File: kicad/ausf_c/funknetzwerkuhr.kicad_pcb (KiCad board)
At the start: 2 copper layers, 170.8 x 131.9 mm, 119 parts, among them J1 Jack-DC, J2 Conn_01x26_Male, J3 Conn_01x26_Female, J4 Conn_01x04_Male, Q1 IRF640, Q10 MMBTA42, Q11 MMBTA42, Q12 MMBTA42, Q13 MMBTA42, Q14 MMBTA42, Q15 MMBTA42, Q16 MMBTA42, Q17 MMBTA42, Q18 MMBTA42, Q19 MMBTA42, Q2 MMBTA42, Q20 MMBTA42, Q21 MMBTA42, Q22 MMBTA42, Q3 MMBTA92, Q4 MMBTA42, Q5 MMBTA92, Q6 MMBTA42, Q7 MMBTA92, Q8 MMBTA42, Q9 MMBTA92, T1 IN-12, T2 IN-12, T3 IN-12, T4 IN-12, U1 74HC595, U10 THERMAL_VIA, U11 THERMAL_VIA, U12 THERMAL_VIA, U13 THERMAL_VIA, U14 THERMAL_VIA, U15 THERMAL_VIA, U16 THERMAL_VIA, U2 74HC595, U3 74HC595, U4 max1771, U5 NCP1117-33G, U6 ESP-12E, U7 THERMAL_VIA, U8 THERMAL_VIA, U9 THERMAL_VIA

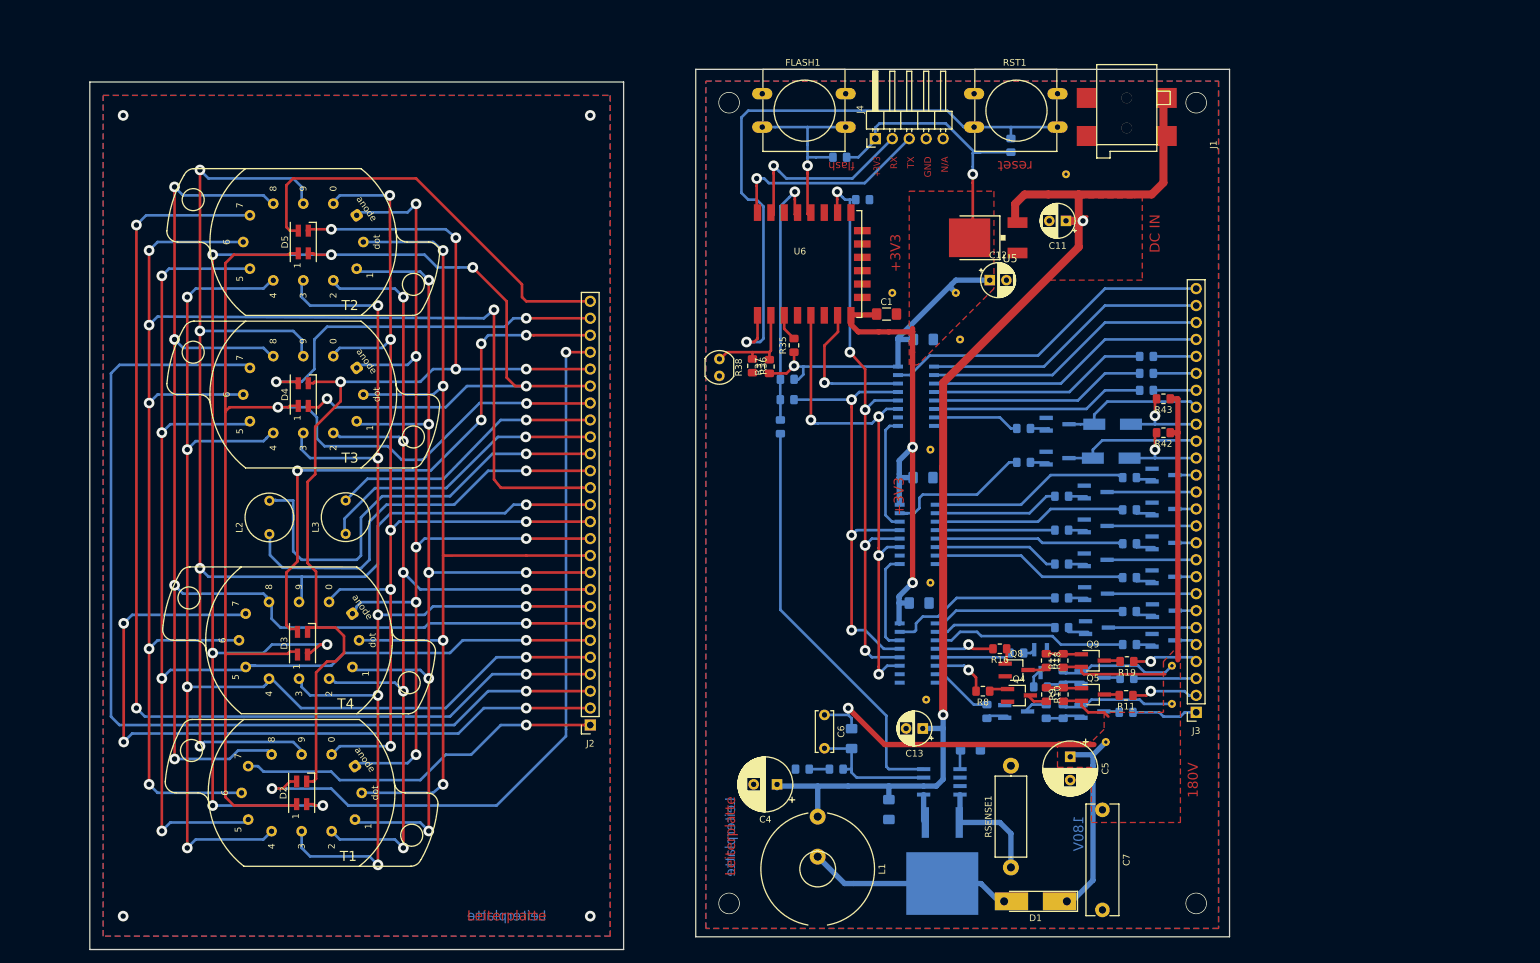
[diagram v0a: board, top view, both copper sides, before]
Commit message: PSU does not fit into the outline.
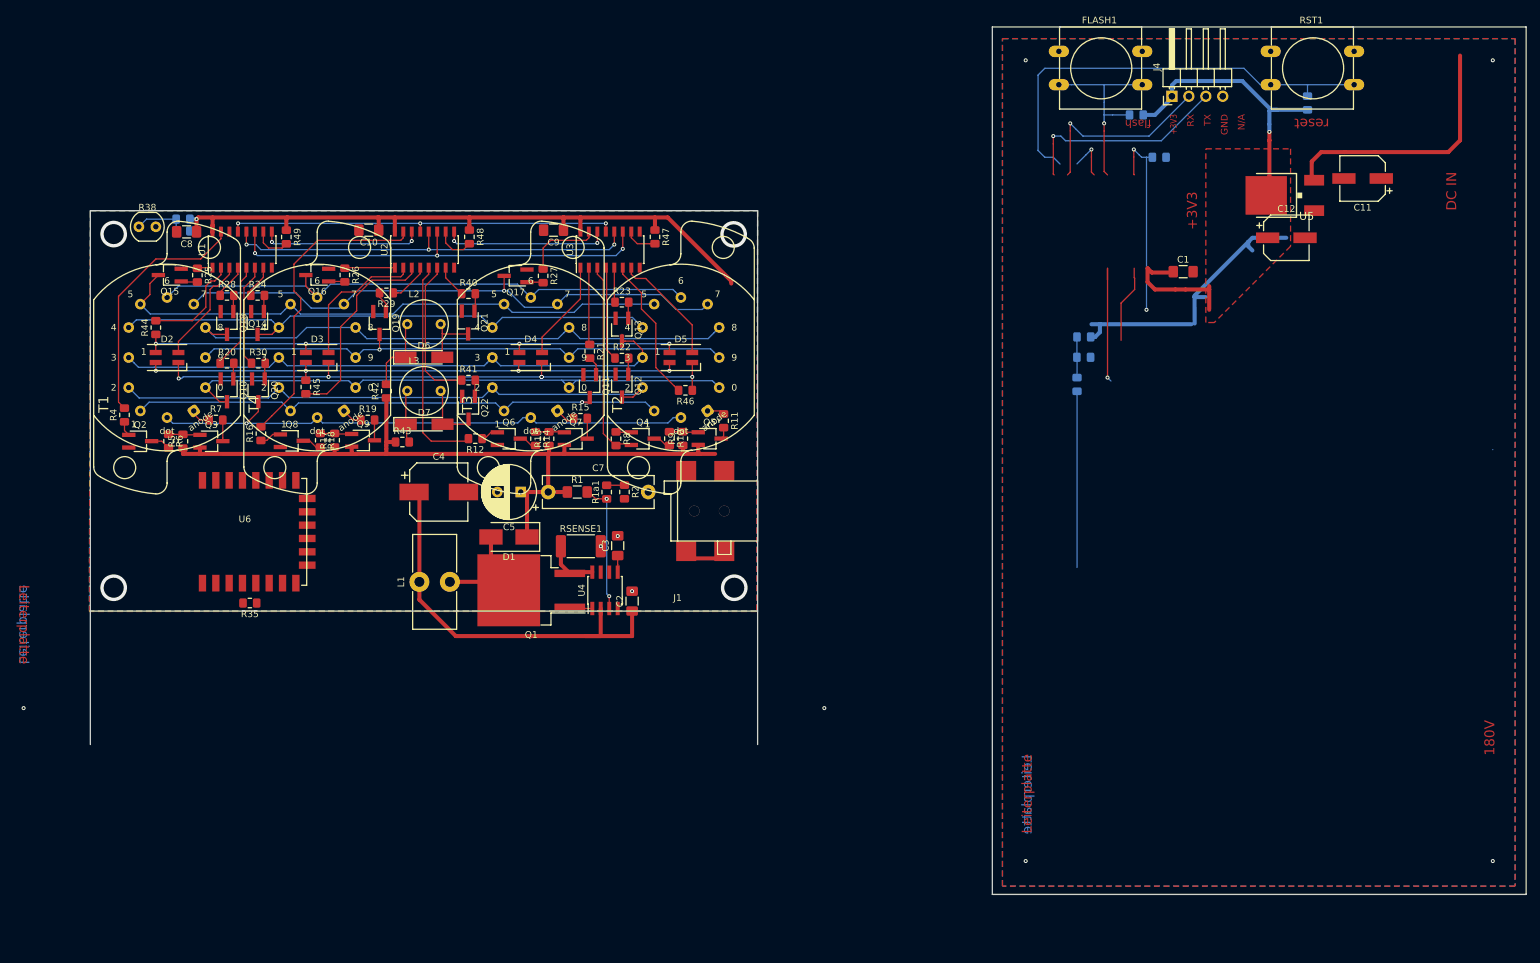
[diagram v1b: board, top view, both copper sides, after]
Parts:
- removed C13: 10uF,25V, Capacitor_THT:CP_Radial_D5.0mm_P2.50mm
- removed C6: 100p 1kV, Capacitor_THT:C_Disc_D6.0mm_W2.5mm_P5.00mm
- removed J2: Conn_01x26_Male, Connector_PinSocket_2.54mm:PinSocket_1x26_P2.54mm_Vertical
- removed J3: Conn_01x26_Female, Connector_PinSocket_2.54mm:PinSocket_1x26_P2.54mm_Vertical
- removed U10, U11, U12, U13, U14, U15, U16, U7, U8, U9: THERMAL_VIA, PartsStash_RW:Thermal_Via
- added R47: 10k, Resistor_SMD:R_0805_2012Metric_Pad1.15x1.40mm_HandSolder, F.Cu at (134.6, 58.9)
- added R48: 10k, Resistor_SMD:R_0805_2012Metric_Pad1.15x1.40mm_HandSolder, F.Cu at (106.8, 58.9)
- added R49: 10k, Resistor_SMD:R_0805_2012Metric_Pad1.15x1.40mm_HandSolder, F.Cu at (79.4, 58.9)
- C10, C2, C3, C8, C9, D6, D7, Q1, Q10, Q11, Q12, Q13, Q14, Q15, Q16, Q17, Q18, Q19, Q2, Q20, Q21, Q22, Q3, Q6, Q7, R1, R12, R13, R14, R15, R1a1, R2, R20, R21, R22, R23, R24, R25, R26, R27, R28, R29, R30, R4, R40, R41, R44, R45, R46, R5, R6, R7, U1, U2, U3, U4: moved to F.Cu
- C11, C12: footprint Capacitor_THT:CP_Radial_D5.0mm_P2.50mm -> Capacitor_SMD:CP_Elec_6.3x5.4
- C4: footprint Capacitor_THT:CP_Radial_D8.0mm_P3.50mm -> Capacitor_SMD:CP_Elec_8x10.5
- D1: footprint Parts:D_MELF-RM10_Universal_Handsoldering -> Diode_SMD:D_SMB_Handsoldering
- J4: footprint Connector_PinHeader_2.54mm:PinHeader_1x05_P2.54mm_Horizontal -> Connector_PinHeader_2.54mm:PinHeader_1x04_P2.54mm_Horizontal
- L1: footprint PartsStash_RW:L_Toroid_Horizontal_D16.8mm_P6mm_AliExpress -> Inductor_THT:L_Toroid_Vertical_L14.0mm_W6.3mm_P4.57mm_Pulse_A
- R36, R37: moved to B.Cu
- RSENSE1: footprint Resistor_THT:R_Axial_DIN0414_L11.9mm_D4.5mm_P15.24mm_Horizontal -> Resistor_SMD:R_2512_6332Metric_Pad1.52x3.35mm_HandSolder
- moved R44 148.8 mm to (59.8, 72.5), turned to 90 degrees
- moved Q15 148.7 mm to (61.9, 64.6), turned to 180 degrees
- moved Q18 146.9 mm to (70.5, 71.8), turned to 270 degrees
- moved Q14 143.9 mm to (75.1, 71.8), turned to 270 degrees
- moved R28 143.3 mm to (70.5, 67.7)
- moved R7 143.3 mm to (68.8, 86.4), turned to 0 degrees
- moved Q10 141.5 mm to (70.5, 81.9), turned to 270 degrees
- moved R24 140.8 mm to (75.1, 67.7)
- moved R25 139.9 mm to (66.0, 64.7), turned to 270 degrees
- moved Q3 138.1 mm to (68.1, 89.5)
- moved R5 138.0 mm to (63.9, 89.5), turned to 90 degrees
- moved R6 137.6 mm to (61.7, 89.5), turned to 270 degrees
- moved Q20 137.5 mm to (75.2, 81.9), turned to 270 degrees
- moved Q2 137.4 mm to (57.5, 89.5)
- moved R20 137.0 mm to (70.5, 77.9)
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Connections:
- net Net-(Q1-Pad3) renamed /hv_psu/SENSE
- net Net-(R33-Pad1) renamed /~OE
- net Net-(U1-Pad9) renamed /SERIAL_U2
- net Net-(U2-Pad9) renamed /SERIAL_U3
- D2 pad 1: Net-(D2-Pad1) -> /RED
- D2 pad 2: Net-(D2-Pad2) -> /DRIVE_LED_A1
- D2 pad 3: Net-(D2-Pad3) -> /GREEN
- D2 pad 4: Net-(D2-Pad4) -> /BLUE
- D3 pad 1: Net-(D2-Pad1) -> /RED
- D3 pad 2: Net-(D3-Pad2) -> /DRIVE_LED_A2
- D3 pad 3: Net-(D2-Pad3) -> /GREEN
- D3 pad 4: Net-(D2-Pad4) -> /BLUE
- D4 pad 1: Net-(D2-Pad1) -> /RED
- D4 pad 2: Net-(D4-Pad2) -> /DRIVE_LED_A3
- D4 pad 3: Net-(D2-Pad3) -> /GREEN
- D4 pad 4: Net-(D2-Pad4) -> /BLUE
- D5 pad 1: Net-(D2-Pad1) -> /RED
- D5 pad 2: Net-(D5-Pad2) -> /DRIVE_LED_A4
- D5 pad 3: Net-(D2-Pad3) -> /GREEN
- D5 pad 4: Net-(D2-Pad4) -> /BLUE
- L2 pad 1: Net-(J2-Pad16) -> /ANODE_N1
- L2 pad 2: Net-(J2-Pad17) -> /CATHODE_N1
- L3 pad 1: Net-(J2-Pad18) -> /ANODE_N2
- L3 pad 2: Net-(J2-Pad19) -> /CATHODE_N2
- R11 pad 1: /A2 -> /A4
- R16 pad 2: /DRIVE_A4 -> /DRIVE_A2
- R19 pad 1: /A4 -> /A2
- R8 pad 2: /DRIVE_A2 -> /DRIVE_A4
- T1 pad 1: /front_panel/A1 -> /A1
- T1 pad 10: /front_panel/D2 -> /D2
- T1 pad 11: /front_panel/D1 -> /D1
- T1 pad 12: /front_panel/DOT -> /DOT
- T1 pad 2: /front_panel/D0 -> /D0
- T1 pad 3: /front_panel/D9 -> /D9
- T1 pad 4: /front_panel/D8 -> /D8
- T1 pad 5: /front_panel/D7 -> /D7
- T1 pad 6: /front_panel/D6 -> /D6
- T1 pad 7: /front_panel/D5 -> /D5
- T1 pad 8: /front_panel/D4 -> /D4
- T1 pad 9: /front_panel/D3 -> /D3
- T2 pad 1: /front_panel/A2 -> /A4
- T2 pad 10: /front_panel/D2 -> /D2
- T2 pad 11: /front_panel/D1 -> /D1
- T2 pad 12: /front_panel/DOT -> /DOT
- T2 pad 2: /front_panel/D0 -> /D0
- T2 pad 3: /front_panel/D9 -> /D9
- T2 pad 4: /front_panel/D8 -> /D8
- T2 pad 5: /front_panel/D7 -> /D7
- T2 pad 6: /front_panel/D6 -> /D6
- T2 pad 7: /front_panel/D5 -> /D5
- T2 pad 8: /front_panel/D4 -> /D4
- T2 pad 9: /front_panel/D3 -> /D3
- T3 pad 1: /front_panel/A3 -> /A3
- T3 pad 10: /front_panel/D2 -> /D2
- T3 pad 11: /front_panel/D1 -> /D1
- T3 pad 12: /front_panel/DOT -> /DOT
- T3 pad 2: /front_panel/D0 -> /D0
- T3 pad 3: /front_panel/D9 -> /D9
- T3 pad 4: /front_panel/D8 -> /D8
- T3 pad 5: /front_panel/D7 -> /D7
- T3 pad 6: /front_panel/D6 -> /D6
- T3 pad 7: /front_panel/D5 -> /D5
- T3 pad 8: /front_panel/D4 -> /D4
- T3 pad 9: /front_panel/D3 -> /D3
- T4 pad 1: /front_panel/A4 -> /A2
- T4 pad 10: /front_panel/D2 -> /D2
- T4 pad 11: /front_panel/D1 -> /D1
- T4 pad 12: /front_panel/DOT -> /DOT
- T4 pad 2: /front_panel/D0 -> /D0
- T4 pad 3: /front_panel/D9 -> /D9
- T4 pad 4: /front_panel/D8 -> /D8
- T4 pad 5: /front_panel/D7 -> /D7
- T4 pad 6: /front_panel/D6 -> /D6
- T4 pad 7: /front_panel/D5 -> /D5
- T4 pad 8: /front_panel/D4 -> /D4
- T4 pad 9: /front_panel/D3 -> /D3
- U1 pad 1: /DRIVE_LED_A3 -> /DRIVE_D5
- U1 pad 10: GND -> Net-(R49-Pad2)
- U1 pad 15: /DRIVE_LED_A4 -> /DRIVE_A1
- U1 pad 2: /DRIVE_LED_A2 -> /DRIVE_RED
- U1 pad 4: /DRIVE_BLUE -> /DRIVE_D8
- U1 pad 5: /DRIVE_GREEN -> /DRIVE_D0
- U1 pad 6: /DRIVE_RED -> /DRIVE_DOT
- U1 pad 7: /DRIVE_S2 -> /DRIVE_D4
- U2 pad 10: GND -> Net-(R48-Pad2)
- U2 pad 15: /DRIVE_S1 -> /DRIVE_A2
- U2 pad 2: /DRIVE_D9 -> /DRIVE_LED_A2
- U2 pad 3: /DRIVE_D0 -> /DRIVE_GREEN
- U2 pad 4: /DRIVE_D7 -> /DRIVE_D9
- U2 pad 5: /DRIVE_DOT -> /DRIVE_A3
- U2 pad 6: /DRIVE_D1 -> /DRIVE_S2
- U2 pad 7: /DRIVE_D2 -> /DRIVE_S1
- U3 pad 1: /DRIVE_D8 -> /DRIVE_LED_A3
- U3 pad 10: GND -> Net-(R47-Pad2)
- U3 pad 15: /DRIVE_D3 -> /DRIVE_D7
- U3 pad 2: /DRIVE_D5 -> /DRIVE_D1
- U3 pad 3: /DRIVE_D4 -> /DRIVE_A4
- U3 pad 4: /DRIVE_A4 -> /DRIVE_D2
- U3 pad 5: /DRIVE_A3 -> /DRIVE_D3
- U3 pad 6: /DRIVE_A2 -> /DRIVE_BLUE
- U3 pad 7: /DRIVE_A1 -> /DRIVE_LED_A4
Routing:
- net Net-(D2-Pad3): track 234.1 -> 0.00 mm, vias 9 -> 0
- net /front_panel/D6: track 230.7 -> 0.00 mm, vias 6 -> 0
- net /front_panel/D9: track 210.7 -> 0.00 mm, vias 5 -> 0
- net /front_panel/D8: track 198.9 -> 0.00 mm, vias 5 -> 0
- net /front_panel/D5: track 191.3 -> 0.00 mm, vias 5 -> 0
- net /front_panel/D4: track 189.5 -> 0.00 mm, vias 5 -> 0
- net Net-(D2-Pad1): track 179.5 -> 0.00 mm, vias 2 -> 0
- net /front_panel/D3: track 173.3 -> 0.00 mm, vias 6 -> 0
- net /front_panel/A4: track 160.9 -> 0.00 mm, vias 3 -> 0
- net /front_panel/D2: track 158.0 -> 0.00 mm, vias 6 -> 0
- net Net-(D2-Pad4): track 157.9 -> 0.00 mm, vias 5 -> 0
- net /front_panel/D1: track 153.7 -> 0.00 mm, vias 6 -> 0
- net /front_panel/DOT: track 152.2 -> 0.00 mm, vias 4 -> 0
- net /front_panel/D0: track 151.5 -> 0.00 mm, vias 6 -> 0
- net Net-(J2-Pad12): track 149.6 -> 0.00 mm, vias 6 -> 0
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- removed copper zone on B.Cu, net (none)
- removed copper zone on F.Cu, net (none)
- removed copper zone on F.Cu, net +9V
- removed copper zone on F.Cu, net 180V
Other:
- board size 170.8 x 131.9 mm -> 215.2 x 130 mm
- net class Default: clearance 0.3 -> 0.1524; trace_width 0.4 -> 0.1524; via_dia 1.6 -> 0.6; via_drill 0.8 -> 0.3
- net class Power added: clearance 0.1524, trace_width 0.6096, via_dia 0.6, via_drill 0.3
- rule trace_clearance: 0.3 -> 0.1524
- rule trace_min: 0.2 -> 0.1524
- rule via_min_size: 0.4 -> 0.6

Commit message: Refactored  - create an abstract superclass
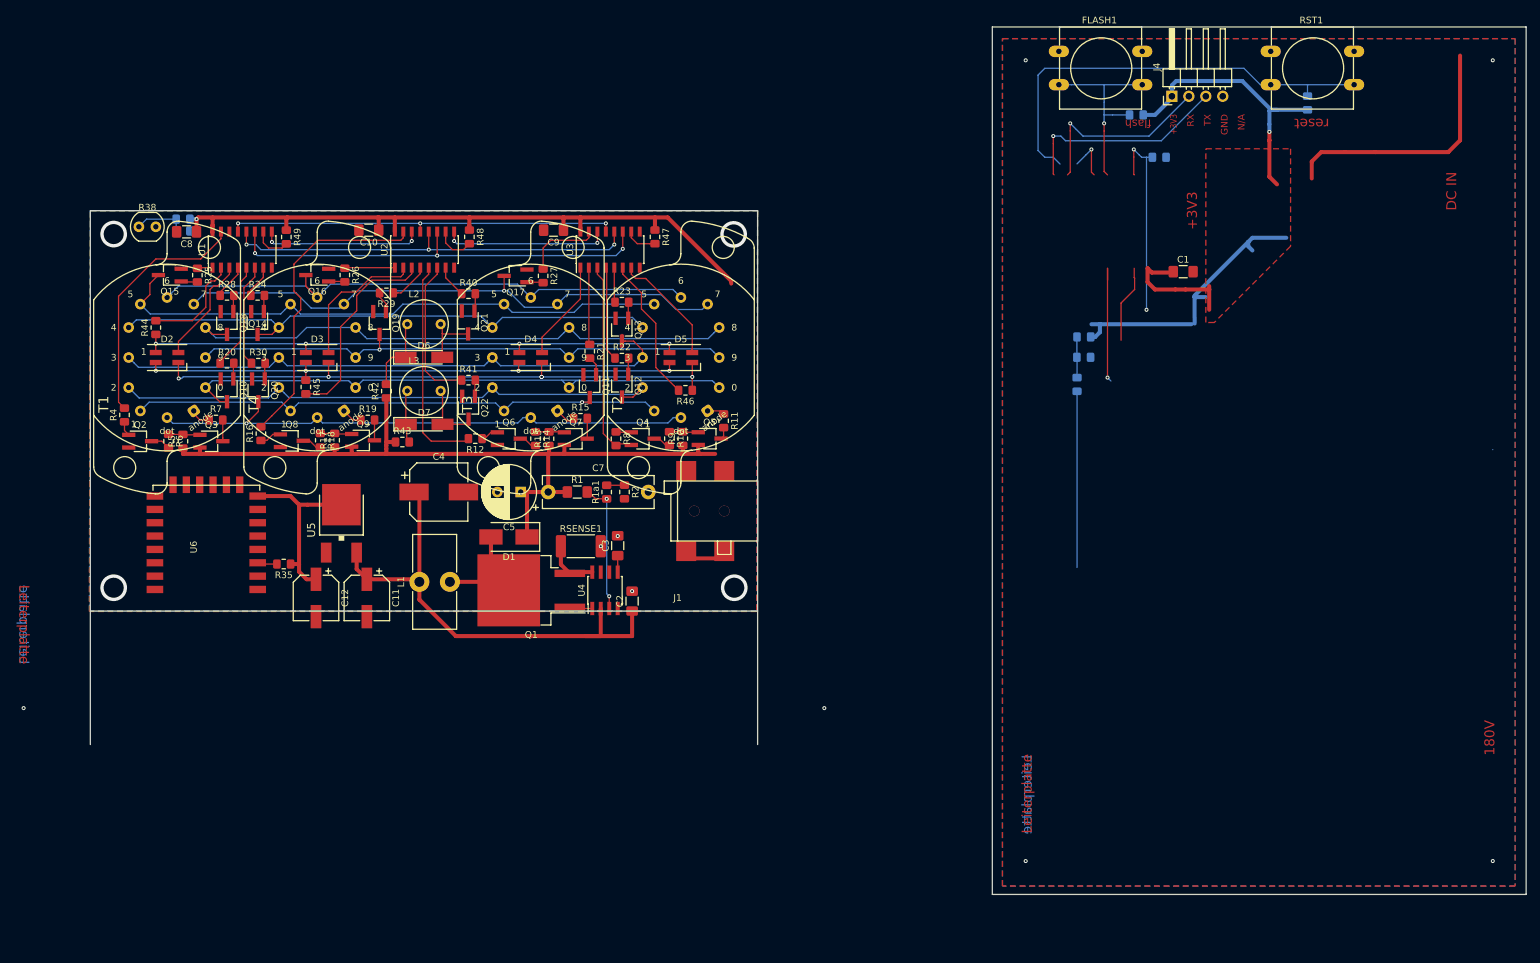
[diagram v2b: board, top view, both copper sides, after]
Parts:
- moved C11 161.9 mm to (91.4, 113.0), turned to 270 degrees
- moved C12 155.1 mm to (83.8, 113.0), turned to 270 degrees
- moved U5 149.2 mm to (87.6, 101.4), turned to 0 degrees
- moved U6 7.76 mm to (74.4, 111.8), turned to 180 degrees
- moved R35 7.74 mm to (79.0, 108.0)
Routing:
- net +3V3: track 207.7 -> 235.9 mm
- net +9V: track 105.3 -> 118.0 mm
- net Net-(R35-Pad2): track 0.00 -> 3.66 mm

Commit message: Nearly done Ausf C PCB layout.
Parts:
- Q10, Q11, Q12, Q13, Q14, Q15, Q16, Q17, Q18, Q19, Q2, Q20, Q21, Q22, Q4, Q6, Q8: footprint Package_TO_SOT_SMD:TSOT-23_HandSoldering -> PartsStash:MPSA42-TSOT-23_HandSoldering
- Q3, Q5, Q7, Q9: footprint Package_TO_SOT_SMD:TSOT-23_HandSoldering -> PartsStash:MPSA92-TSOT-23_HandSoldering
- R1: moved to B.Cu
- R10, R11, R12, R13, R14, R15, R16, R17, R18, R19, R20, R21, R22, R23, R24, R25, R26, R27, R28, R29, R3, R30, R31, R32, R35, R39, R4, R40, R41, R42, R43, R44, R45, R46, R47, R48, R49, R5, R6, R7, R8, R9: footprint Resistor_SMD:R_0805_2012Metric_Pad1.15x1.40mm_HandSolder -> PartsStash:R_0805_2012Metric_Pad1.15x1.40mm_HandSolder_Value
- R1a1, R2: footprint Resistor_SMD:R_0805_2012Metric_Pad1.15x1.40mm_HandSolder -> PartsStash:R_0805_2012Metric_Pad1.15x1.40mm_HandSolder_Value; moved to B.Cu
- R33, R34, R36, R37: footprint Resistor_SMD:R_0805_2012Metric_Pad1.15x1.40mm_HandSolder -> PartsStash:R_0805_2012Metric_Pad1.15x1.40mm_HandSolder_Value; moved to F.Cu
- T1, T2, T3, T4: footprint Parts:IN-12_0.8mm -> PartsStash:IN-12_0.8mm_simple
- moved R31 170.1 mm to (78.7, 111.8), turned to 180 degrees
- moved RST1 167.9 mm to (92.1, 131.1), turned to 180 degrees
- moved R39 161.2 mm to (57.9, 99.8)
- moved R33 148.7 mm to (52.6, 103.4), turned to 270 degrees
- moved R34 147.8 mm to (52.6, 108.2)
- moved R32 142.7 mm to (78.7, 103.8)
- moved C1 139.0 mm to (78.4, 95.8)
- moved J4 137.8 mm to (104.8, 124.3), turned to 270 degrees
- moved R3 124.3 mm to (78.7, 105.8)
- moved FLASH1 123.7 mm to (122.4, 131.1), turned to 180 degrees
- moved R38 73.4 mm to (73.5, 129.0), turned to 180 degrees
- moved R36 66.7 mm to (72.5, 124.2), turned to 180 degrees
- moved R37 55.5 mm to (78.7, 109.7)
- moved J1 12.8 mm to (145.0, 112.8)
- moved C2 7.71 mm to (128.0, 120.5), turned to 0 degrees
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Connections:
- R11 pad 1: /A4 -> Net-(Q5-Pad3)
- R11 pad 2: Net-(Q5-Pad3) -> /A4
- R12 pad 1: Net-(Q6-Pad1) -> /DRIVE_A3
- R12 pad 2: /DRIVE_A3 -> Net-(Q6-Pad1)
- R23 pad 1: /DRIVE_D3 -> Net-(Q13-Pad1)
- R23 pad 2: Net-(Q13-Pad1) -> /DRIVE_D3
- R27 pad 1: /DRIVE_D7 -> Net-(Q17-Pad1)
- R27 pad 2: Net-(Q17-Pad1) -> /DRIVE_D7
- R40 pad 1: /DRIVE_S1 -> Net-(Q21-Pad1)
- R40 pad 2: Net-(Q21-Pad1) -> /DRIVE_S1
- R47 pad 1: +3V3 -> Net-(R47-Pad1)
- R47 pad 2: Net-(R47-Pad2) -> +3V3
- R48 pad 1: +3V3 -> Net-(R48-Pad1)
- R48 pad 2: Net-(R48-Pad2) -> +3V3
- R49 pad 1: +3V3 -> Net-(R49-Pad1)
- R49 pad 2: Net-(R49-Pad2) -> +3V3
- U1 pad 10: Net-(R49-Pad2) -> Net-(R49-Pad1)
- U2 pad 10: Net-(R48-Pad2) -> Net-(R48-Pad1)
- U3 pad 10: Net-(R47-Pad2) -> Net-(R47-Pad1)
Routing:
- net HSPI_MOSI: track 11.7 -> 80.6 mm, vias 0 -> 4
- net /~OE: track 58.8 -> 120.4 mm, vias 3 -> 4
- net Net-(R34-Pad1): track 26.4 -> 87.3 mm, vias 0 -> 2
- net HSPI_CLK: track 83.9 -> 142.0 mm, vias 4 -> 6
- net FLASH: track 30.0 -> 85.8 mm, vias 1 -> 2
- net Net-(J4-Pad2): track 28.9 -> 64.9 mm
- net HSPI_CS: track 92.1 -> 127.2 mm
- net +3V3: track 235.9 -> 269.2 mm, vias 2 -> 9
- net RESET: track 66.0 -> 33.7 mm, vias 0 -> 2
- net +9V: track 118.0 -> 89.2 mm
- net Net-(J4-Pad3): track 31.8 -> 56.8 mm
- net ADC: track 7.84 -> 25.5 mm
- net BLANK: track 13.1 -> 28.6 mm
- net Net-(R1-Pad2): track 19.8 -> 27.3 mm, vias 2 -> 1
- net Net-(R49-Pad1): track 0.00 -> 6.44 mm
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- removed copper zone on F.Cu, net +3V3
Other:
- board size 215.2 x 130 mm -> 100 x 80 mm
- board text removed: "+3V3"
- board text removed: "180V"
- board text removed: "DC IN"
- board text removed: "GND"
- board text removed: "Leiterplatte"
- board text removed: "N/A"
- board text removed: "RX"
- board text removed: "TX"
- board text removed: "flash"
- board text removed: "reset"

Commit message: Ausf C PCB version ordered.
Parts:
- removed C11: 10uF, Capacitor_SMD:CP_Elec_6.3x5.4
- added G***: LOGO, PartsStash:Funknetzwerkuhr_Ausf_C, F.Cu at (136.4, 127.4)
- added J2: Conn_01x04_Male, Connector_PinHeader_2.54mm:PinHeader_1x04_P2.54mm_Vertical, F.Cu at (66.5, 124.3)
- added J3: 180V, Connector_PinHeader_2.54mm:PinHeader_1x02_P2.54mm_Vertical, F.Cu at (141.5, 95.9)
- C12: footprint Capacitor_SMD:CP_Elec_6.3x5.4 -> Capacitor_THT:CP_Radial_D6.3mm_P2.50mm
- C4: value 100uF,25V -> 220uF,25V; footprint Capacitor_SMD:CP_Elec_8x10.5 -> Capacitor_THT:CP_Radial_D10.0mm_P2.50mm_P5.00mm
- R3, R31, R32, R39: moved to F.Cu
- moved C12 17.9 mm to (84.8, 98.9), turned to 90 degrees
- moved R31 6.75 mm to (83.3, 116.7)
- moved R39 6.41 mm to (57.0, 93.5)
- moved R35 5.38 mm to (84.1, 107.8)
- moved R32 5.32 mm to (84.1, 103.8)
- moved U5 4.32 mm to (91.9, 101.4)
- moved C5 3.44 mm to (111.6, 99.1), turned to 90 degrees
- moved C2 3.32 mm to (129.3, 117.5)
- moved FLASH1 2.21 mm to (122.4, 128.9)
- moved RST1 2.21 mm to (92.1, 128.9)
- moved C4 1.84 mm to (101.6, 98.9), turned to 90 degrees
- moved C1 0.85 mm to (78.1, 95.0)
- moved R3 0.13 mm to (78.9, 105.8)
- moved R37 0.13 mm to (78.9, 109.7)
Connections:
- net Net-(J4-Pad2) renamed /RXD
- net Net-(J4-Pad3) renamed /TXD
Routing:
- net HSPI_CLK: track 142.0 -> 177.8 mm
- net HSPI_MOSI: track 80.6 -> 115.7 mm
- net HSPI_CS: track 127.2 -> 157.8 mm, vias 5 -> 4
- net /RXD: track 64.9 -> 51.9 mm
- net Net-(R34-Pad1): track 87.3 -> 99.8 mm
- net FLASH: track 85.8 -> 73.6 mm
- net +3V3: track 269.2 -> 278.0 mm, vias 9 -> 6
- net Net-(R1-Pad2): track 27.3 -> 20.2 mm
- net 180V: track 120.2 -> 126.9 mm
- net /TXD: track 56.8 -> 50.4 mm
- net Net-(R35-Pad2): track 3.82 -> 10.2 mm
- net +9V: track 89.2 -> 83.7 mm
- net RESET: track 33.7 -> 36.2 mm
- net BLANK: track 28.6 -> 30.3 mm, vias 1 -> 3
- net GND: vias 43 -> 27
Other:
- board text added: "+3V3"
- board text added: "CLK"
- board text added: "CS"
- board text added: "ESP12e"
- board text added: "FLASH"
- board text added: "GND"
- board text added: "HSPI"
- board text added: "MOSI"
- board text added: "RESET"
- board text added: "RXD"
- board text added: "TXD"
